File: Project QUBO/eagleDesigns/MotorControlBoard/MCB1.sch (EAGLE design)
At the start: 13 parts, among them U1 PCA9685

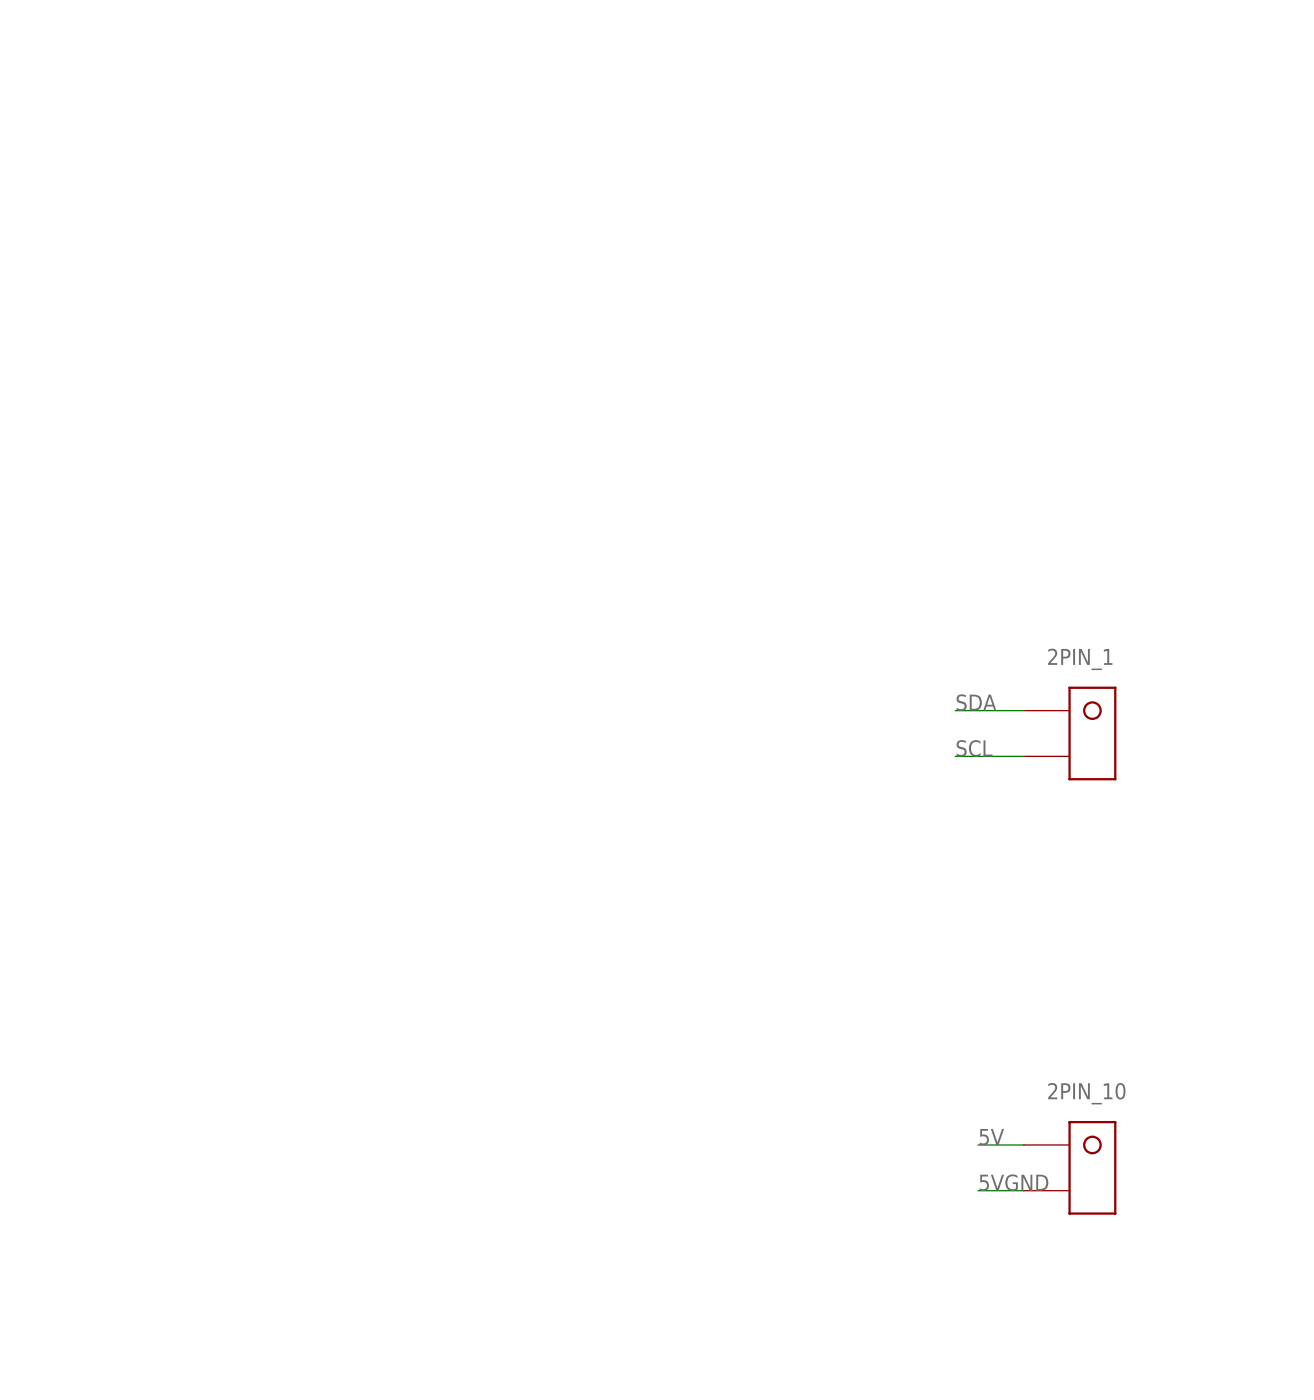
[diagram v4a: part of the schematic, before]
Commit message: added LED placeholder
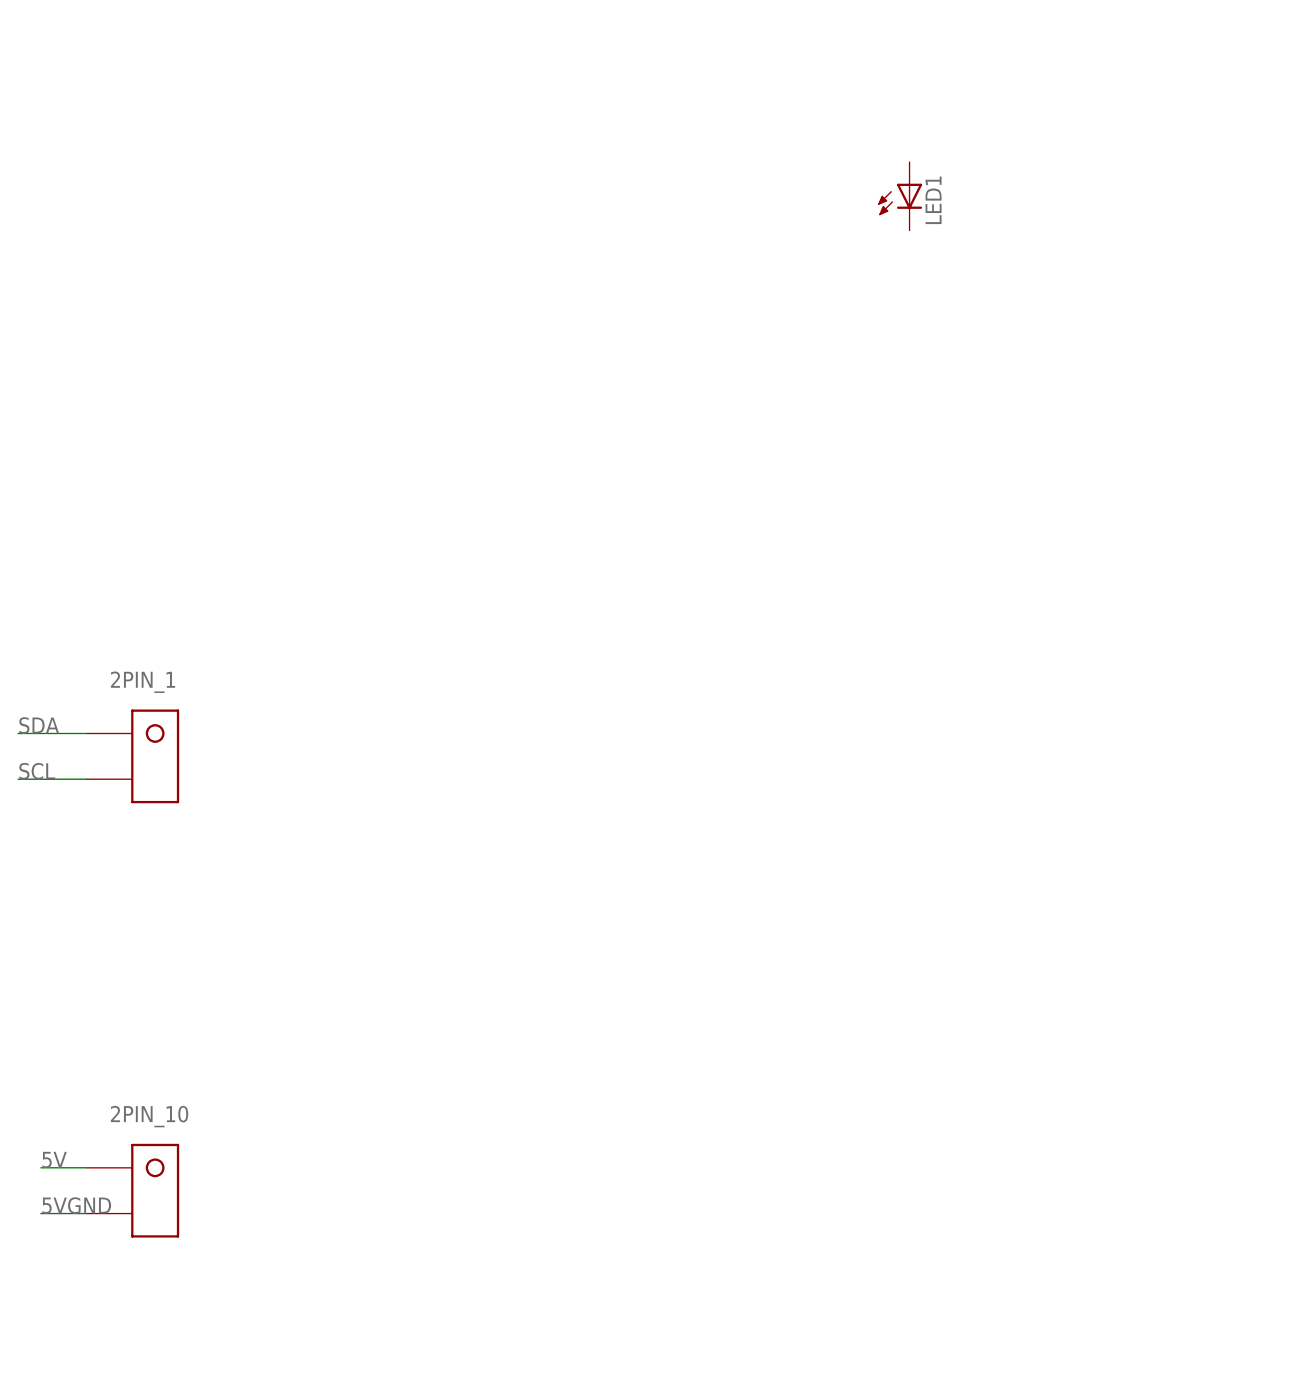
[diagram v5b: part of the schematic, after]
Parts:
- added LED1: (no value), led:LEDCHIPLED_0805
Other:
- moved on the sheet: 2PIN_1, 2PIN_10
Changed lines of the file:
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@@
 <part name="2PIN_9" library="molex" deviceset="KK254_VERT_2PIN" device="22-29-2021"/>
 <part name="2PIN_10" library="molex" deviceset="KK254_VERT_2PIN" device="22-29-2021"/>
+<part name="LED1" library="led" deviceset="LED" device="CHIPLED_0805"/>
 </parts>
 <sheets>
@@
 <instance part="U$1" gate="G$1" x="-35.56" y="40.64"/>
 <instance part="U$2" gate="G$1" x="-38.1" y="157.48"/>
-<instance part="2PIN_1" gate="U1" x="-114.3" y="73.66"/>
+<instance part="2PIN_1" gate="U1" x="-218.44" y="71.12"/>
 <instance part="2PIN_2" gate="U1" x="66.04" y="132.08"/>
 <instance part="2PIN_3" gate="U1" x="101.6" y="132.08"/>
@@
 <instance part="2PIN_8" gate="U1" x="66.04" y="-53.34"/>
 <instance part="2PIN_9" gate="U1" x="101.6" y="-53.34"/>
-<instance part="2PIN_10" gate="U1" x="-114.3" y="25.4"/>
+<instance part="2PIN_10" gate="U1" x="-218.44" y="22.86"/>
+<instance part="LED1" gate="G$1" x="-134.62" y="134.62"/>
 </instances>
 <busses>
@@
 <segment>
 <pinref part="2PIN_1" gate="U1" pin="P$2"/>
-<wire x1="-121.92" y1="71.12" x2="-129.54" y2="71.12" width="0.1524" layer="91"/>
-<label x="-129.54" y="71.12" size="1.778" layer="95"/>
+<wire x1="-226.06" y1="68.58" x2="-233.68" y2="68.58" width="0.1524" layer="91"/>
+<label x="-233.68" y="68.58" size="1.778" layer="95"/>
 </segment>
 <segment>
@@
 <segment>
 <pinref part="2PIN_1" gate="U1" pin="P$1"/>
-<wire x1="-121.92" y1="76.2" x2="-129.54" y2="76.2" width="0.1524" layer="91"/>
-<label x="-129.54" y="76.2" size="1.778" layer="95"/>
+<wire x1="-226.06" y1="73.66" x2="-233.68" y2="73.66" width="0.1524" layer="91"/>
+<label x="-233.68" y="73.66" size="1.778" layer="95"/>
 </segment>
 <segment>
@@
 <segment>
 <pinref part="2PIN_10" gate="U1" pin="P$1"/>
-<wire x1="-121.92" y1="27.94" x2="-127" y2="27.94" width="0.1524" layer="91"/>
-<label x="-127" y="27.94" size="1.778" layer="95"/>
+<wire x1="-226.06" y1="25.4" x2="-231.14" y2="25.4" width="0.1524" layer="91"/>
+<label x="-231.14" y="25.4" size="1.778" layer="95"/>
 </segment>
 <segment>
@@
 <segment>
 <pinref part="2PIN_10" gate="U1" pin="P$2"/>
-<wire x1="-121.92" y1="22.86" x2="-127" y2="22.86" width="0.1524" layer="91"/>
-<label x="-127" y="22.86" size="1.778" layer="95"/>
+<wire x1="-226.06" y1="20.32" x2="-231.14" y2="20.32" width="0.1524" layer="91"/>
+<label x="-231.14" y="20.32" size="1.778" layer="95"/>
 </segment>
 <segment>

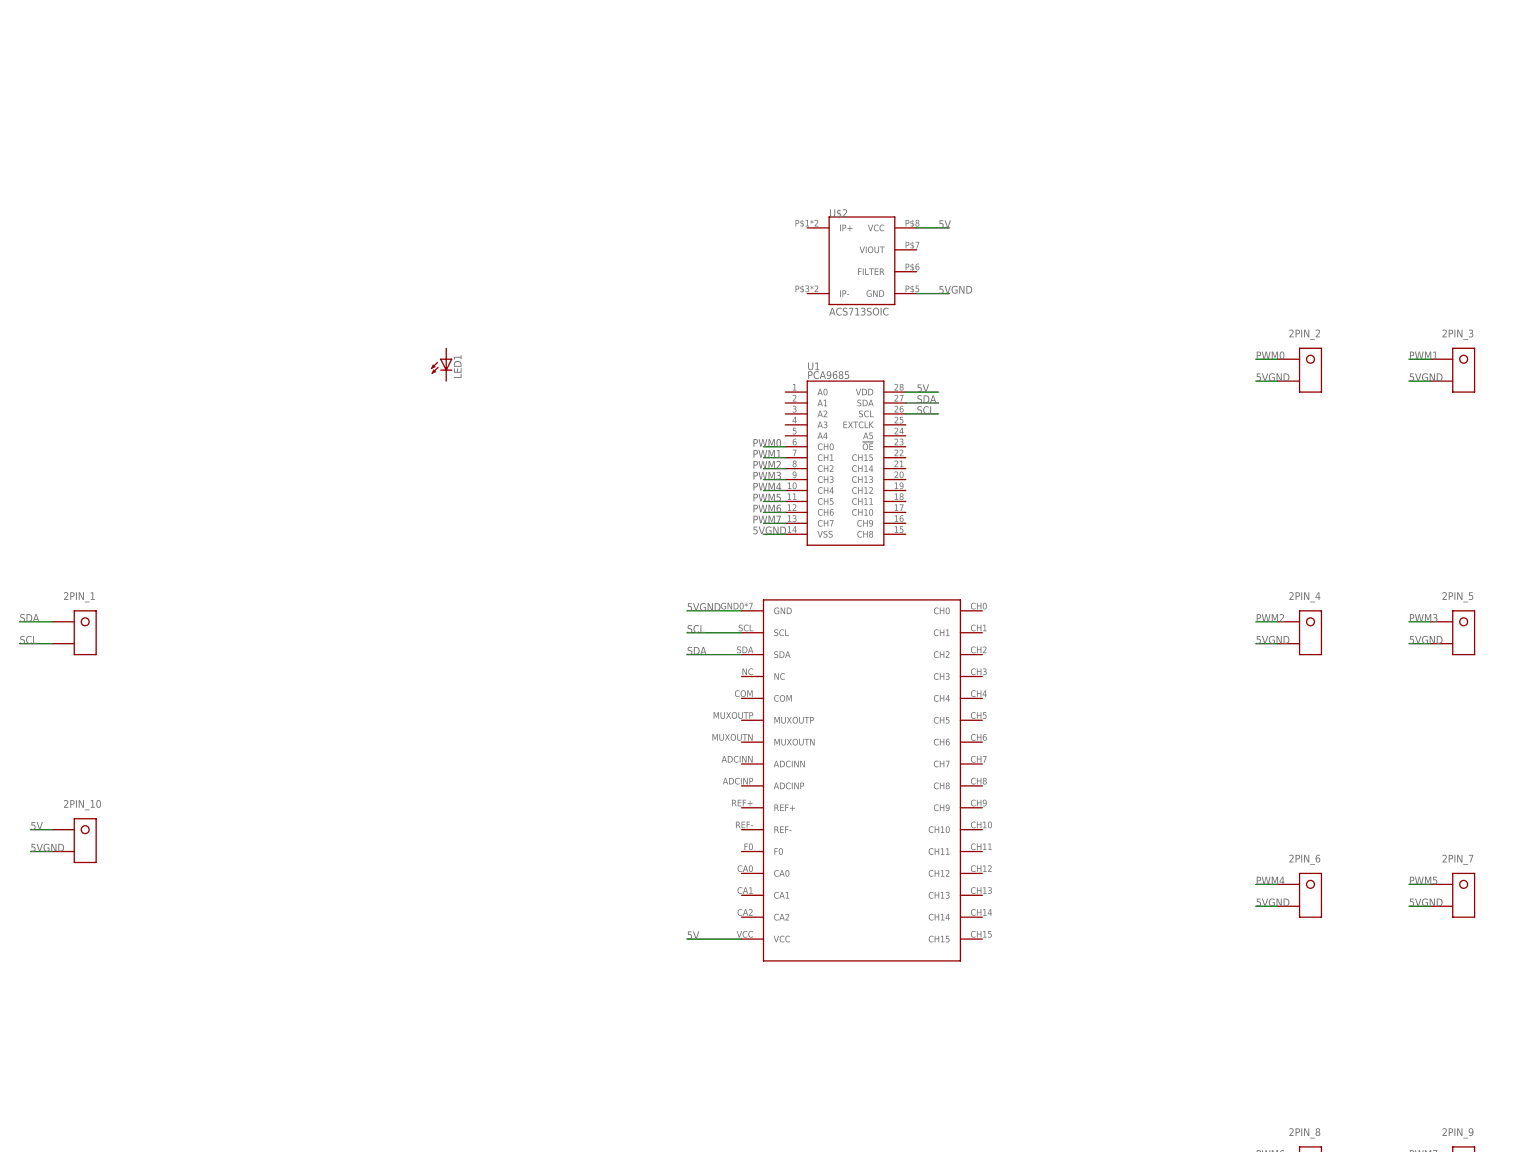
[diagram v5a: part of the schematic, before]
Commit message: update to motor control board
linked current sensor to header, ADC, for one motor. added ultrafit
(motor power) and supersabre (batery power) headers
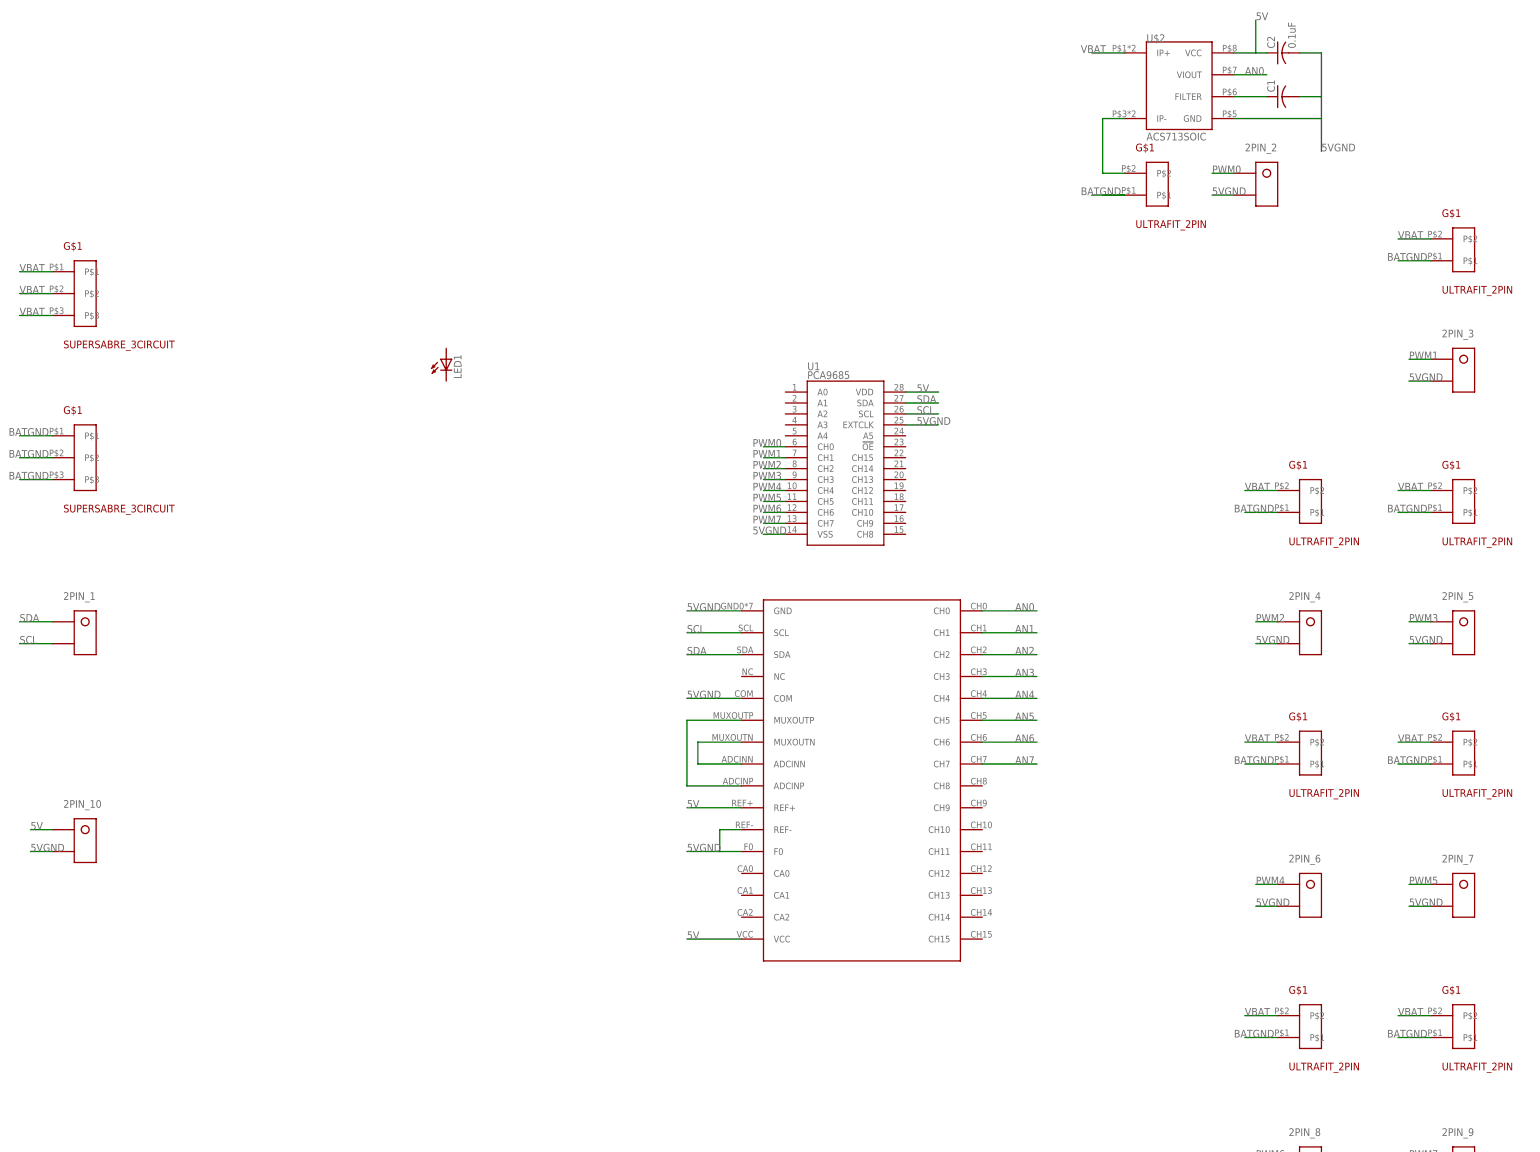
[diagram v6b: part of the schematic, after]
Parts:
- added C1: (no value), resistor:C-USC0805
- added C2: 0.1uF, resistor:C-USC0805
- added U$10, U$11, U$12, U$5, U$6, U$7, U$8, U$9: ULTRAFIT_2PIN, molex:ULTRAFIT_2PIN
- added U$3, U$4: SUPERSABRE_3CIRCUIT, molex:SUPERSABRE_3CIRCUIT
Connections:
- new net AN0: U$1.CH0, U$2.VIOUT
- new net AN1: U$1.CH1
- new net AN2: U$1.CH2
- new net AN3: U$1.CH3
- new net AN4: U$1.CH4
- new net AN5: U$1.CH5
- new net AN6: U$1.CH6
- new net AN7: U$1.CH7
- new net BATGND: U$10.P$1, U$11.P$1, U$12.P$1, U$3.P$1, U$3.P$2, U$3.P$3, U$5.P$1, U$6.P$1, U$7.P$1, U$8.P$1, U$9.P$1
- new net N$1: C1.1, U$2.FILTER
- new net N$2: U$2.IP-, U$5.P$2
- new net N$3: U$1.ADCINP, U$1.MUXOUTP
- new net N$4: U$1.ADCINN, U$1.MUXOUTN
- new net VBAT: U$10.P$2, U$11.P$2, U$12.P$2, U$2.IP+, U$4.P$1, U$4.P$2, U$4.P$3, U$6.P$2, U$7.P$2, U$8.P$2, U$9.P$2
- net 5V: now also C2.1, U$1.REF+
- net 5VGND: now also C1.2, C2.2, U$1.COM, U$1.F0, U$1.REF-, U1.EXTCLK
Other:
- moved on the sheet: 2PIN_2, U$2

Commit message: update to MCB
need to finalize pinouts on ADC and PWM controller, filer capacitors on
current sensors, fuses
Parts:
- removed 2PIN_5: (no value), molex:KK254_VERT_2PIN22-29-2021
- removed U$10, U$9: ULTRAFIT_2PIN, molex:ULTRAFIT_2PIN
- added 2PIN_11: (no value), molex:KK254_VERT_2PIN22-29-2021
- added C11, C14, C16, C18, C4, C6, C8: (no value), resistor:C-USC0805
- added C12, C13, C15, C17, C3, C5, C7: 0.1uF, resistor:C-USC0805
- added F1, F2, F3, F4, F5, F6, F7, F8, F9: FUSEX20MM, molex:FUSEX20MM
- added LED2, LED3, LED4, LED5, LED6, LED7, LED8: (no value), led:LEDCHIPLED_0805
- added R10, R3, R4, R5, R6, R7, R8, R9: 100, resistor:R-US_R0805
- added U$13, U$15, U$17, U$19, U$21: ACS713SOIC, allegro:ACS713SOIC
- added U$14, U$16, U$18, U$20: ULTRAFIT_2PIN, molex:ULTRAFIT_2PIN
- U$11, U$8: value ULTRAFIT_2PIN -> ACS713SOIC; device molex:ULTRAFIT_2PIN -> allegro:ACS713SOIC
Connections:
- new net N$10: C4.1, U$13.FILTER
- new net N$11: F1.2, U$4.P$1, U$4.P$2, U$4.P$3
- new net N$12: F2.2, U$2.IP+
- new net N$13: C11.1, U$11.FILTER
- new net N$14: U$11.IP-, U$12.P$2
- new net N$15: U$16.P$2, U$17.IP-
- new net N$16: C14.1, U$17.FILTER
- new net N$17: U$18.P$2, U$19.IP-
- new net N$18: C16.1, U$19.FILTER
- new net N$19: U$20.P$2, U$21.IP-
- new net N$20: C18.1, U$21.FILTER
- new net N$21: F3.2
- new net N$22: F4.2
- new net N$23: R4.1, U1.CH14
- new net N$24: R10.1, U1.CH8
- new net N$25: F5.2
- new net N$26: F6.2, U$11.IP+
- new net N$27: R7.1, U1.CH11
- new net N$28: R9.1, U1.CH9
- new net N$29: R8.1, U1.CH10
- new net N$30: R6.1, U1.CH12
- new net N$31: R5.1, U1.CH13
- new net N$32: R3.1, U1.CH15
- new net N$33: F7.2, U$17.IP+
- new net N$34: F8.2, U$19.IP+
- new net N$35: F9.2, U$21.IP+
- new net N$36: LED1.A, R3.2
- new net N$37: LED2.A, R4.2
- new net N$38: LED3.A, R5.2
- new net N$39: LED4.A, R6.2
- new net N$40: LED5.A, R7.2
- new net N$41: LED6.A, R8.2
- new net N$42: LED7.A, R9.2
- new net N$43: LED8.A, R10.2
- new net N$5: U$14.P$2, U$15.IP-
- new net N$6: U$13.IP-, U$6.P$2
- new net N$7: C6.1, U$15.FILTER
- new net N$8: U$7.P$2, U$8.IP-
- new net N$9: C8.1, U$8.FILTER
- net 5V: now also C12.1, C13.1, C15.1, C17.1, C3.1, C5.1, C7.1, U$11.VCC, U$13.VCC, U$15.VCC, U$17.VCC, U$19.VCC, U$21.VCC, U$8.VCC
- net 5VGND: now also 2PIN_11.P$2, C11.2, C12.2, C13.2, C14.2, C15.2, C16.2, C17.2, C18.2, C3.2, C4.2, C5.2, C6.2, C7.2, C8.2, LED1.C, LED2.C, LED3.C, LED4.C, LED5.C, LED6.C, LED7.C, LED8.C, U$11.GND, U$13.GND, U$15.GND, U$17.GND, U$19.GND, U$21.GND, U$8.GND; no longer 2PIN_5.P$2
- net AN1: now also U$13.VIOUT
- net AN2: now also U$15.VIOUT
- net AN3: now also U$8.VIOUT
- net AN4: now also U$11.VIOUT
- net AN5: now also U$17.VIOUT
- net AN6: now also U$19.VIOUT
- net AN7: now also U$21.VIOUT
- net BATGND: now also U$14.P$1, U$16.P$1, U$18.P$1, U$20.P$1; no longer U$10.P$1, U$11.P$1, U$8.P$1, U$9.P$1
- net PWM2: now also 2PIN_11.P$1; no longer 2PIN_4.P$1
- net PWM3: now also 2PIN_4.P$1; no longer 2PIN_5.P$1
- net VBAT: now also F1.1, F2.1, F3.1, F4.1, F5.1, F6.1, F7.1, F8.1, F9.1; no longer U$10.P$2, U$11.P$2, U$12.P$2, U$2.IP+, U$4.P$1, U$4.P$2, U$4.P$3, U$6.P$2, U$7.P$2, U$8.P$2, U$9.P$2
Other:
- moved on the sheet: 2PIN_1, 2PIN_10, 2PIN_2, 2PIN_3, 2PIN_4, 2PIN_6, 2PIN_7, 2PIN_8, 2PIN_9, C1, C2, LED1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
